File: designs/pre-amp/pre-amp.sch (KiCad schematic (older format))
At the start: 23 parts

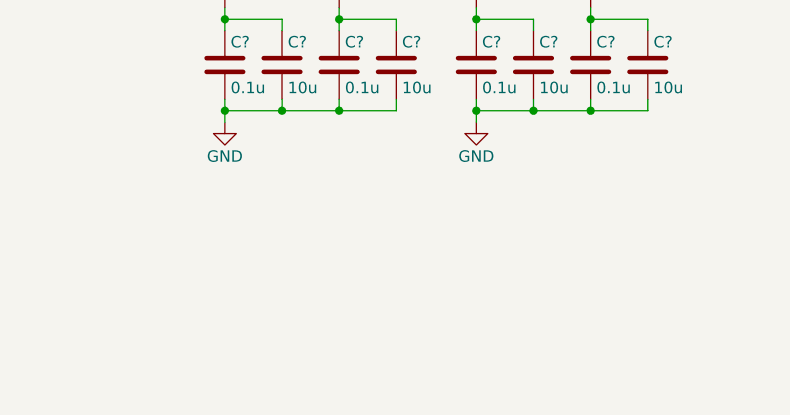
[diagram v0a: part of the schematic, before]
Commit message: [designs/pre-amp] power connectors
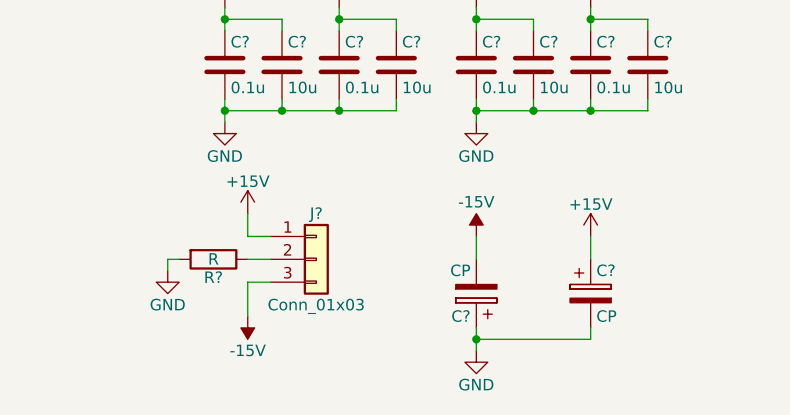
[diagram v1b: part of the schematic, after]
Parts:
- added C? (x2): CP, symbol CP
- added J?: Conn_01x03, symbol Conn_01x03
- added R?: R, symbol R
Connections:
- net +15V: now also C?.1, J?.1 (Pin_1)
- net -15V: now also C?.2, J?.3 (Pin_3)
- net GND: now also C?.1, C?.2, R?.2
- new net: J?.2 (Pin_2), R?.1
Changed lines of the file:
@@
 	1    0    0    -1
 $EndComp
+$Comp
+L Conn_01x03 J?
+U 1 1 5AEB6541
+P 1750 3550
+F 0 "J?" H 1750 3750 50  0000 C CNN
+F 1 "Conn_01x03" H 1750 3350 50  0000 C CNN
+F 2 "" H 1750 3550 50  0001 C CNN
+F 3 "" H 1750 3550 50  0001 C CNN
+	1    1750 3550
+	1    0    0    -1
+$EndComp
+$Comp
+L R R?
+U 1 1 5AEB681A
+P 1300 3550
+F 0 "R?" V 1380 3550 50  0000 C CNN
+F 1 "R" V 1300 3550 50  0000 C CNN
+F 2 "" V 1230 3550 50  0001 C CNN
+F 3 "" H 1300 3550 50  0001 C CNN
+	1    1300 3550
+	0    1    1    0
+$EndComp
+$Comp
+L GND #PWR?
+U 1 1 5AEB68A7
+P 1100 3600
+F 0 "#PWR?" H 1100 3350 50  0001 C CNN
+F 1 "GND" H 1100 3450 50  0000 C CNN
+F 2 "" H 1100 3600 50  0001 C CNN
+F 3 "" H 1100 3600 50  0001 C CNN
+	1    1100 3600
+	1    0    0    -1
+$EndComp
+$Comp
+L -15V #PWR?
+U 1 1 5AEB68FD
+P 1450 3800
+F 0 "#PWR?" H 1450 3900 50  0001 C CNN
+F 1 "-15V" H 1450 3950 50  0000 C CNN
+F 2 "" H 1450 3800 50  0001 C CNN
+F 3 "" H 1450 3800 50  0001 C CNN
+	1    1450 3800
+	-1   0    0    1
+$EndComp
+$Comp
+L +15V #PWR?
+U 1 1 5AEB69C1
+P 1450 3350
+F 0 "#PWR?" H 1450 3200 50  0001 C CNN
+F 1 "+15V" H 1450 3490 50  0000 C CNN
+F 2 "" H 1450 3350 50  0001 C CNN
+F 3 "" H 1450 3350 50  0001 C CNN
+	1    1450 3350
+	1    0    0    -1
+$EndComp
+Wire Wire Line
+	1450 3350 1450 3450
+Wire Wire Line
+	1450 3450 1550 3450
+Wire Wire Line
+	1450 3550 1550 3550
+Wire Wire Line
+	1550 3650 1450 3650
+Wire Wire Line
+	1450 3650 1450 3800
+Wire Wire Line
+	1150 3550 1100 3550
+Wire Wire Line
+	1100 3550 1100 3600
+$Comp
+L GND #PWR?
+U 1 1 5AEB6FED
+P 2450 3950
+F 0 "#PWR?" H 2450 3700 50  0001 C CNN
+F 1 "GND" H 2450 3800 50  0000 C CNN
+F 2 "" H 2450 3950 50  0001 C CNN
+F 3 "" H 2450 3950 50  0001 C CNN
+	1    2450 3950
+	1    0    0    -1
+$EndComp
+$Comp
+L -15V #PWR?
+U 1 1 5AEB6FF3
+P 2450 3450
+F 0 "#PWR?" H 2450 3550 50  0001 C CNN
+F 1 "-15V" H 2450 3600 50  0000 C CNN
+F 2 "" H 2450 3450 50  0001 C CNN
+F 3 "" H 2450 3450 50  0001 C CNN
+	1    2450 3450
+	1    0    0    -1
+$EndComp
+$Comp
+L +15V #PWR?
+U 1 1 5AEB6FF9
+P 2950 3450
+F 0 "#PWR?" H 2950 3300 50  0001 C CNN
+F 1 "+15V" H 2950 3590 50  0000 C CNN
+F 2 "" H 2950 3450 50  0001 C CNN
+F 3 "" H 2950 3450 50  0001 C CNN
+	1    2950 3450
+	1    0    0    -1
+$EndComp
+$Comp
+L CP C?
+U 1 1 5AEB7242
+P 2950 3700
+F 0 "C?" H 2975 3800 50  0000 L CNN
+F 1 "CP" H 2975 3600 50  0000 L CNN
+F 2 "" H 2988 3550 50  0001 C CNN
+F 3 "" H 2950 3700 50  0001 C CNN
+	1    2950 3700
+	1    0    0    -1
+$EndComp
+$Comp
+L CP C?
+U 1 1 5AEB72B5
+P 2450 3700
+F 0 "C?" H 2475 3800 50  0000 L CNN
+F 1 "CP" H 2475 3600 50  0000 L CNN
+F 2 "" H 2488 3550 50  0001 C CNN
+F 3 "" H 2450 3700 50  0001 C CNN
+	1    2450 3700
+	-1   0    0    1
+$EndComp
+Wire Wire Line
+	2950 3450 2950 3550
+Wire Wire Line
+	2950 3850 2950 3900
+Wire Wire Line
+	2950 3900 2450 3900
+Wire Wire Line
+	2450 3850 2450 3950
+Connection ~ 2450 3900
+Wire Wire Line
+	2450 3550 2450 3450
 $EndSCHEMATC
